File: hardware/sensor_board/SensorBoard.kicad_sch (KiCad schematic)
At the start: 28 parts, among them J1 EXT, J10 LED L2, J11 LED L3, J12 LED R1, J13 LED R2, J14 SPARE GPIO, J15 VSYS BUS, J16 GND BUS, J17 3V3 BUS, J2 SOIL SENSOR L, J3 SOIL SENSOR R, J4 ENV SENSOR L, J5 ENV SENSOR R, J6 FEED SENSOR L, J7 FEED SENSOR R, J8 LED R3, J9 LED L1, U1 Pico, U2 74HC595

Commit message: Brand new sensor board, includes I2C expander, RTC and relay board connections
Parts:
- added BT1: CR1220, Battery:BatteryHolder_Keystone_3000_1x12mm, symbol Device:Battery_Cell
- added C2: 0.1uf, Capacitor_THT:C_Disc_D6.0mm_W2.5mm_P5.00mm, symbol Device:C
- added D1, D2: 1N5820, Diode_THT:D_DO-201AD_P15.24mm_Horizontal, symbol Diode:1N5820
- added J1: Relay Board, Connector_PinHeader_2.54mm:PinHeader_1x10_P2.54mm_Vertical, symbol Connector_Generic:Conn_01x10
- added J15: LED L1, Connector_JST:JST_XH_B2B-XH-A_1x02_P2.50mm_Vertical, symbol Connector_Generic:Conn_02x01
- added J16: LED L2, Connector_JST:JST_XH_B2B-XH-A_1x02_P2.50mm_Vertical, symbol Connector_Generic:Conn_02x01
- added J2: Pi, Connector_JST:JST_XH_B2B-XH-A_1x02_P2.50mm_Vertical, symbol Connector:Screw_Terminal_01x02
- added J24: Raspberry Pi GPIO header, Connector_PinHeader_2.54mm:PinHeader_2x20_P2.54mm_Vertical, symbol Connector:Raspberry_Pi_2_3
- added J25: RTC Header, Connector_PinHeader_2.54mm:PinHeader_1x05_P2.54mm_Vertical, symbol Connector_Generic:Conn_01x05
- added J26: I2C3, Connector_JST:JST_XH_B4B-XH-A_1x04_P2.50mm_Vertical, symbol Connector_Generic:Conn_01x04
- added J27: I2C2, Connector_JST:JST_XH_B4B-XH-A_1x04_P2.50mm_Vertical, symbol Connector_Generic:Conn_01x04
- added J28: I2C1, Connector_JST:JST_XH_B4B-XH-A_1x04_P2.50mm_Vertical, symbol Connector_Generic:Conn_01x04
- added J29: I2C4, Connector_JST:JST_XH_B4B-XH-A_1x04_P2.50mm_Vertical, symbol Connector_Generic:Conn_01x04
- added J3: Display, Connector_JST:JST_XH_B2B-XH-A_1x02_P2.50mm_Vertical, symbol Connector:Screw_Terminal_01x02
- added J30: I2C5, Connector_JST:JST_XH_B4B-XH-A_1x04_P2.50mm_Vertical, symbol Connector_Generic:Conn_01x04
- added J31: I2C6, Connector_JST:JST_XH_B4B-XH-A_1x04_P2.50mm_Vertical, symbol Connector_Generic:Conn_01x04
- added J32: I2C7, Connector_JST:JST_XH_B4B-XH-A_1x04_P2.50mm_Vertical, symbol Connector_Generic:Conn_01x04
- added J4: DC IN 5V, Connector_BarrelJack:BarrelJack_Horizontal, symbol Connector:Barrel_Jack
- added Q1, Q2, Q3, Q4, Q5, Q6, Q7, Q8: PN2222A, Package_TO_SOT_THT:TO-92_Inline, symbol Transistor_BJT:PN2222A
- added R1, R2, R3, R4, R5, R6, R7, R8: 2.2k, Resistor_THT:R_Axial_DIN0207_L6.3mm_D2.5mm_P7.62mm_Horizontal, symbol Device:R
- added R11, R12: R1, Resistor_THT:R_Axial_DIN0207_L6.3mm_D2.5mm_P7.62mm_Horizontal, symbol Device:R
- added R19, R20: 4.3k, Resistor_THT:R_Axial_DIN0207_L6.3mm_D2.5mm_P7.62mm_Horizontal, symbol Device:R
- added RN1, RN2: 10k, Resistor_THT:R_Array_SIP9, symbol Device:R_Network08
- added SW1: Reset, Button_Switch_THT:SW_PUSH_6mm, symbol Switch:SW_Push
- added U3: TCA9548A, Package_DIP:DIP-24_W15.24mm, symbol Interface_Expansion:TCA9548A_Adafruit
- added U4: LM1117, Package_TO_SOT_THT:TO-220-3_Horizontal_TabDown, symbol Regulator_Linear:LM1117-3.3
- added U5: DS3231MZ, Package_SO:SOIC-8_3.9x4.9mm_P1.27mm, symbol Timer_RTC:DS3231MZ
- J12: renamed from J4; value ENV SENSOR L -> DHT22 R
- J14: renamed from J5; value ENV SENSOR R -> DHT22 L
- J17: renamed from J8; value LED R3 -> LED L3
- J18: renamed from J9; value LED L1 -> LED L4
- J19: renamed from J10; value LED L2 -> LED R1
- J21: renamed from J11; value LED L3 -> LED R2
- J22: renamed from J12; value LED R1 -> LED R3
- J23: renamed from J13; value LED R2 -> LED R4
- U1: value Pico -> Raspberry Pico
- renumbered J16 to J10, J7 to J11, J14 to J13, J1 to J20, J15 to J5, J2 to J6, J17 to J7, J6 to J8, J3 to J9, R8 to R10, R1 to R13, R2 to R14, R3 to R15, R4 to R16, R5 to R17, R6 to R18, R7 to R9
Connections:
- net +3V3: now also J26.1 (Pin_1), J27.1 (Pin_1), J28.1 (Pin_1), J29.1 (Pin_1), J30.1 (Pin_1), J31.1 (Pin_1), J32.1 (Pin_1), U3.1 (VCC), U4.2 (VO); no longer U1.36 (3V3)
- net CTL RX: now also J24.8 (GPIO14/TXD)
- net CTL TX: now also J24.10 (GPIO15/RXD)
- net ENV SENSOR L CTL: now also J14.2 (Pin_2), R10.1, U1.20 (GPIO15); no longer J12.2 (Pin_2), R9.1, U1.19 (GPIO14)
- net ENV SENSOR R CTL: now also J12.2 (Pin_2), R9.1, U1.19 (GPIO14); no longer J14.2 (Pin_2), R10.1, U1.20 (GPIO15)
- net GND: now also BT1.2 (-), C2.2, J1.1 (Pin_1), J15.1 (Pin_1), J16.1 (Pin_1), J2.2 (Pin_2), J24.14 (GND), J24.20 (GND), J24.25 (GND), J24.30 (GND), J24.34 (GND), J24.39 (GND), J24.6 (GND), J24.9 (GND), J25.1 (Pin_1), J26.4 (Pin_4), J27.4 (Pin_4), J28.4 (Pin_4), J29.4 (Pin_4), J3.2 (Pin_2), J30.4 (Pin_4), J31.4 (Pin_4), J32.4 (Pin_4), J4.2, Q1.1 (E), Q2.1 (E), Q3.1 (E), Q4.1 (E), Q5.1 (E), Q6.1 (E), Q7.1 (E), Q8.1 (E), RN1.1 (common), SW1.1, U3.2 (GND), U4.1 (GND), U5.5 (GND)
- net I2C1 SCL: now also U3.4 (SCL); no longer J6.5 (Pin_5), J9.5 (Pin_5)
- net I2C1 SDA: now also U3.3 (SDA); no longer J6.2 (Pin_2), J9.2 (Pin_2)
- net VS: now also D1.1 (K), D2.1 (K), J1.10 (Pin_10), J2.1 (Pin_1), J3.1 (Pin_1), RN2.1 (common), U4.3 (VI); no longer J20.1 (Pin_1)
- net at U2.1 (QB): now also R12.1
- net at U2.15 (QA): now also R11.1
- net at U1.30 (RUN): now also SW1.2
- net ENV SENSOR L DETECT renamed DHT22 L DETECT
- net DHT22 L DETECT: now also J14.4 (Pin_4); no longer J12.4 (Pin_4)
- net ENV SENSOR R DETECT renamed DHT22 R DETECT
- net DHT22 R DETECT: now also J12.4 (Pin_4); no longer J14.4 (Pin_4)
- new net: Q6.2 (B), R6.2
- new net: J1.7 (Pin_7), Q6.3 (C), RN2.4 (R3)
- new net: J15.2 (Pin_2), R11.2
- new net: Q1.2 (B), R1.2
- new net: J1.2 (Pin_2), Q1.3 (C), RN2.9 (R8)
- new net: J32.2 (Pin_2), U3.23 (SD7)
- new net: J32.3 (Pin_3), U3.24 (SC7)
- new net: J16.2 (Pin_2), R12.2
- new net: J1.9 (Pin_9), Q8.3 (C), RN2.2 (R1)
- new net: J1.8 (Pin_8), Q7.3 (C), RN2.3 (R2)
- new net: J1.6 (Pin_6), Q5.3 (C), RN2.5 (R4)
- new net: J1.5 (Pin_5), Q4.3 (C), RN2.6 (R5)
- new net: J1.4 (Pin_4), Q3.3 (C), RN2.7 (R6)
- new net: J1.3 (Pin_3), Q2.3 (C), RN2.8 (R7)
- new net: J24.40 (GPIO21/SCLK1), R8.1, RN1.9 (R8)
- new net: Q8.2 (B), R8.2
- new net: BT1.1 (+), U5.6 (VBAT)
- new net: J24.32 (PWM0/GPIO12), R2.1, RN1.3 (R2)
- new net: Q2.2 (B), R2.2
- new net: J6.2 (Pin_2), J9.2 (Pin_2), U3.9 (SD0)
- new net: J6.5 (Pin_5), J9.5 (Pin_5), U3.10 (SC0)
- new net: J29.2 (Pin_2), U3.17 (SD4)
- new net: J29.3 (Pin_3), U3.18 (SC4)
- new net: J28.2 (Pin_2), U3.11 (SD1)
- new net: J28.3 (Pin_3), U3.12 (SC1)
- new net: J26.2 (Pin_2), U3.15 (SD3)
- new net: J26.3 (Pin_3), U3.16 (SC3)
- new net: C2.1, J24.1 (3V3), J25.5 (Pin_5), R19.1, R20.1, U5.2 (VCC)
- new net: J24.5 (SCL/GPIO3), J25.3 (Pin_3), R20.2, U5.8 (SCL)
- new net: J27.2 (Pin_2), U3.13 (SD2)
- new net: J27.3 (Pin_3), U3.14 (SC2)
- new net: J30.2 (Pin_2), U3.19 (SD5)
- new net: J30.3 (Pin_3), U3.20 (SC5)
- new net: J31.2 (Pin_2), U3.21 (SD6)
- new net: J31.3 (Pin_3), U3.22 (SC6)
- new net: J24.29 (GCLK1/GPIO5), R1.1, RN1.2 (R1)
- new net: J24.3 (SDA/GPIO2), J25.4 (Pin_4), R19.2, U5.7 (SDA)
- new net: J24.31 (GCLK2/GPIO6), R3.1, RN1.4 (R3)
- new net: J24.33 (PWM1/GPIO13), R4.1, RN1.5 (R4)
- new net: J24.35 (GPIO19/MISO1), R6.1, RN1.7 (R6)
- new net: J24.36 (GPIO16), R5.1, RN1.6 (R5)
- new net: J24.38 (GPIO20/MOSI1), R7.1, RN1.8 (R7)
- new net: Q3.2 (B), R3.2
- new net: Q7.2 (B), R7.2
- new net: D2.2 (A), J4.1
- new net: Q4.2 (B), R4.2
- new net: Q5.2 (B), R5.2
- new net VSYS: D1.2 (A), J20.1 (Pin_1)
- no-connect marks 8 -> 33
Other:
- moved on the sheet: C1, J10, J11, J12, J13, J14, J17, J18, J19, J20, J21, J22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

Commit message: New version without DHT22. Full exposed I2C expander
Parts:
- removed J12: DHT22 R, Connector_JST:JST_XH_B4B-XH-A_1x04_P2.50mm_Vertical, symbol Connector_Generic:Conn_01x04
- removed J14: DHT22 L, Connector_JST:JST_XH_B4B-XH-A_1x04_P2.50mm_Vertical, symbol Connector_Generic:Conn_01x04
- removed R10: R8, Resistor_THT:R_Axial_DIN0207_L6.3mm_D2.5mm_P7.62mm_Horizontal, symbol Device:R
- removed R9: R7, Resistor_THT:R_Axial_DIN0207_L6.3mm_D2.5mm_P7.62mm_Horizontal, symbol Device:R
- added C3: 0.1uf, Capacitor_THT:C_Disc_D6.0mm_W2.5mm_P5.00mm, symbol Device:C
- added J26: I2C0, Connector_JST:JST_XH_B5B-XH-A_1x05_P2.50mm_Vertical, symbol Connector_Generic:Conn_01x05
- added RN3: 10k, Resistor_THT:R_Array_SIP9, symbol Device:R_Network08
- added U6: 74HC165, Package_DIP:DIP-16_W7.62mm, symbol 74xx:74HC165
- J13: footprint Connector_PinHeader_2.54mm:PinHeader_1x05_P2.54mm_Vertical -> Connector_PinHeader_2.54mm:PinHeader_1x04_P2.54mm_Vertical; symbol Connector_Generic:Conn_01x05 -> Connector_Generic:Conn_01x04
- J27: renamed from J28; footprint Connector_JST:JST_XH_B4B-XH-A_1x04_P2.50mm_Vertical -> Connector_JST:JST_XH_B5B-XH-A_1x05_P2.50mm_Vertical; symbol Connector_Generic:Conn_01x04 -> Connector_Generic:Conn_01x05
- J28: renamed from J27; footprint Connector_JST:JST_XH_B4B-XH-A_1x04_P2.50mm_Vertical -> Connector_JST:JST_XH_B5B-XH-A_1x05_P2.50mm_Vertical; symbol Connector_Generic:Conn_01x04 -> Connector_Generic:Conn_01x05
- J29: renamed from J26; footprint Connector_JST:JST_XH_B4B-XH-A_1x04_P2.50mm_Vertical -> Connector_JST:JST_XH_B5B-XH-A_1x05_P2.50mm_Vertical; symbol Connector_Generic:Conn_01x04 -> Connector_Generic:Conn_01x05
- J30: renamed from J29; footprint Connector_JST:JST_XH_B4B-XH-A_1x04_P2.50mm_Vertical -> Connector_JST:JST_XH_B5B-XH-A_1x05_P2.50mm_Vertical; symbol Connector_Generic:Conn_01x04 -> Connector_Generic:Conn_01x05
- J31: renamed from J30; footprint Connector_JST:JST_XH_B4B-XH-A_1x04_P2.50mm_Vertical -> Connector_JST:JST_XH_B5B-XH-A_1x05_P2.50mm_Vertical; symbol Connector_Generic:Conn_01x04 -> Connector_Generic:Conn_01x05
- J32: renamed from J31; footprint Connector_JST:JST_XH_B4B-XH-A_1x04_P2.50mm_Vertical -> Connector_JST:JST_XH_B5B-XH-A_1x05_P2.50mm_Vertical; symbol Connector_Generic:Conn_01x04 -> Connector_Generic:Conn_01x05
- J33: renamed from J32; footprint Connector_JST:JST_XH_B4B-XH-A_1x04_P2.50mm_Vertical -> Connector_JST:JST_XH_B5B-XH-A_1x05_P2.50mm_Vertical; symbol Connector_Generic:Conn_01x04 -> Connector_Generic:Conn_01x05
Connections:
- net DHT22 L DETECT is gone; now on an unnamed net: U1.6 (GPIO4)
- net DHT22 R DETECT is gone; now on an unnamed net: U1.7 (GPIO5)
- net +3V3: now also C3.1, J26.1 (Pin_1), RN3.1 (common), U6.16 (VCC)
- net GND: now also J27.5 (Pin_5), J28.5 (Pin_5), J29.5 (Pin_5), J30.5 (Pin_5), J31.5 (Pin_5), J32.5 (Pin_5), J33.5 (Pin_5), C3.2, J26.5 (Pin_5), U6.10 (DS), U6.15 (~{CE}), U6.8 (GND); no longer J27.4 (Pin_4), J28.4 (Pin_4), J29.4 (Pin_4), J30.4 (Pin_4), J31.4 (Pin_4), J32.4 (Pin_4), J33.4 (Pin_4)
- net at J6.2 (Pin_2), J9.2 (Pin_2): no longer U3.9 (SD0)
- net at J6.5 (Pin_5), J9.5 (Pin_5): no longer U3.10 (SC0)
- net ENV SENSOR L CTL renamed GPIO15
- net GPIO15: now also J13.4 (Pin_4)
- net ENV SENSOR R CTL: no longer names the net of U1.19 (GPIO14)
- net ENV SENSOR R CTL: now also U6.1 (~{PL})
- net GPIO10: no longer names the net of U1.14 (GPIO10)
- net GPIO10: now also U6.9 (Q7); no longer J13.5 (Pin_5)
- net GPIO11: no longer names the net of U1.15 (GPIO11)
- net GPIO11: now also U6.2 (CP); no longer J13.4 (Pin_4)
- new net: J33.4 (Pin_4), RN3.2 (R1), U6.6 (D7)
- new net: J26.4 (Pin_4), RN3.9 (R8), U6.11 (D0)
- new net: J27.4 (Pin_4), RN3.8 (R7), U6.12 (D1)
- new net: J28.4 (Pin_4), RN3.7 (R6), U6.13 (D2)
- new net: J29.4 (Pin_4), RN3.6 (R5), U6.14 (D3)
- new net: J30.4 (Pin_4), RN3.5 (R4), U6.3 (D4)
- new net: J31.4 (Pin_4), RN3.4 (R3), U6.4 (D5)
- new net: J32.4 (Pin_4), RN3.3 (R2), U6.5 (D6)
- new net: J26.3 (Pin_3), U3.10 (SC0)
- new net: J26.2 (Pin_2), U3.9 (SD0)
- no-connect marks 33 -> 34
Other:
- moved on the sheet: BT1, C1, C2, D1, D2, J1, J10, J11, J15, J16, J17, J18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

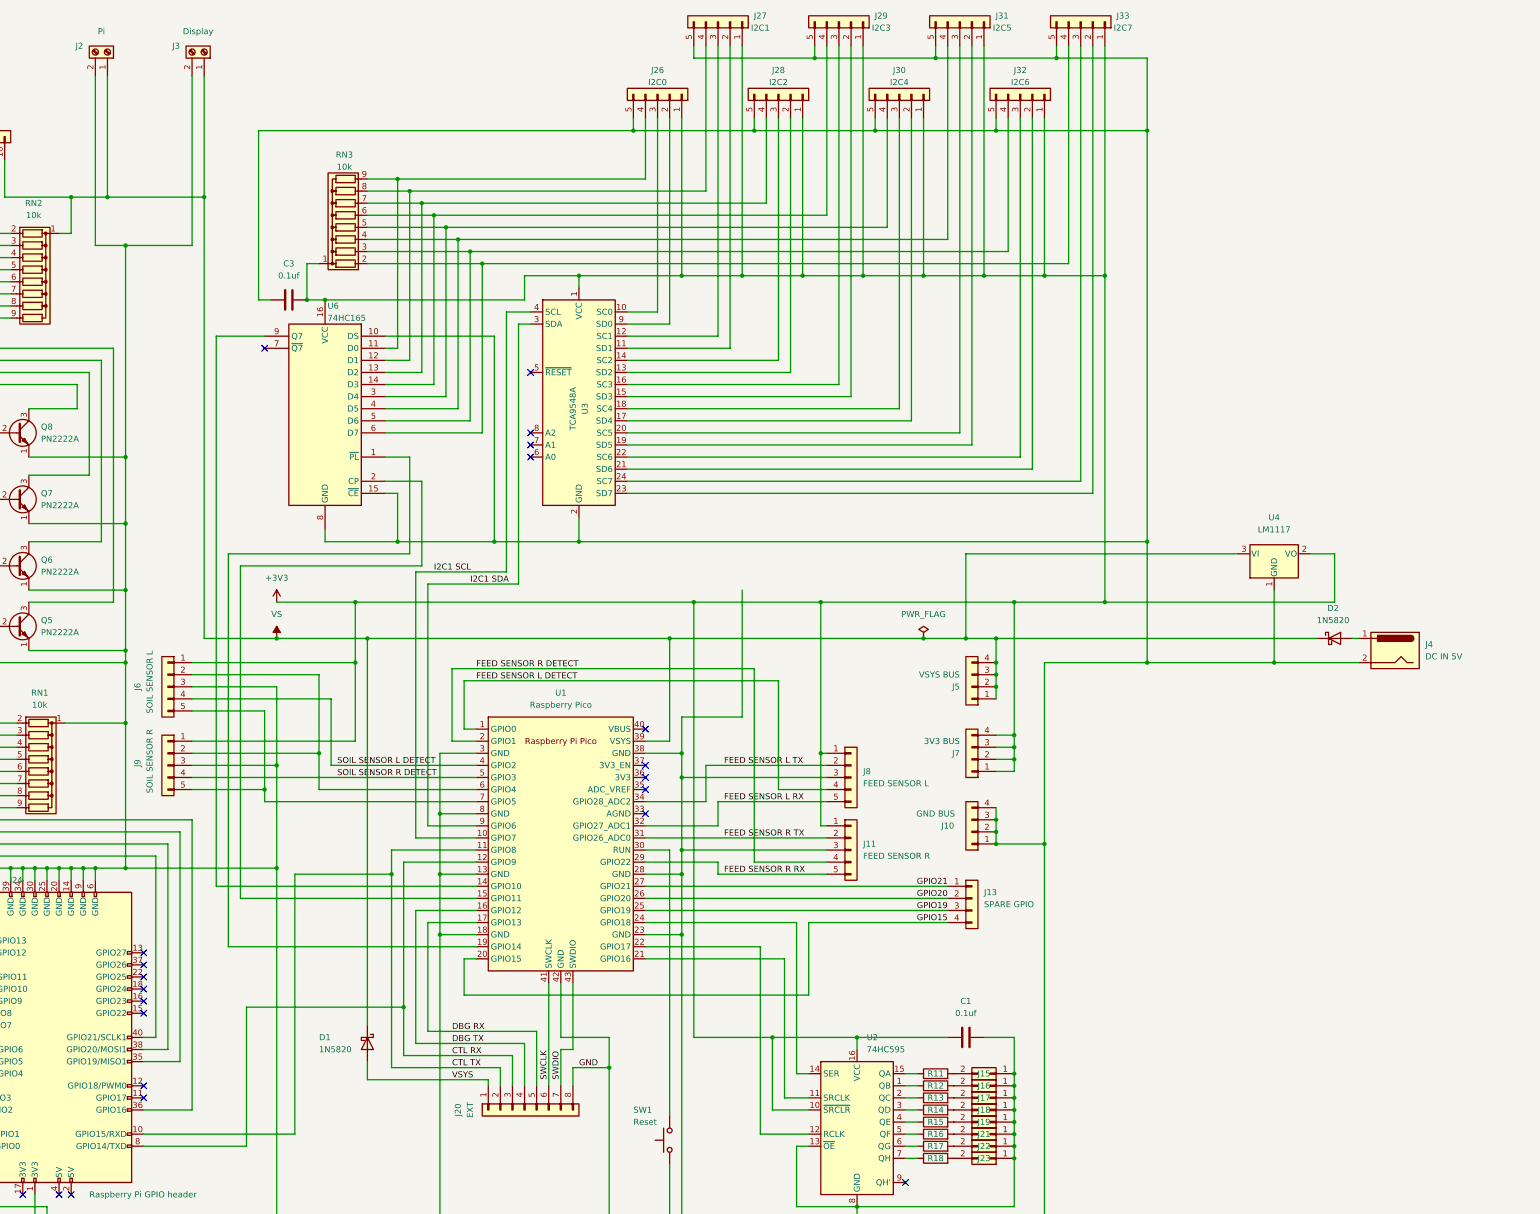
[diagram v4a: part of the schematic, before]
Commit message: Completely revamped board. Will fully use the I2C expander now to have one "sensor pod" per grow system containing an SCD30 and a soil sensor. This allows for 8 sensor pods. Will reuse the I2C interface for the soil sensors for additional feed level sonar sensors.
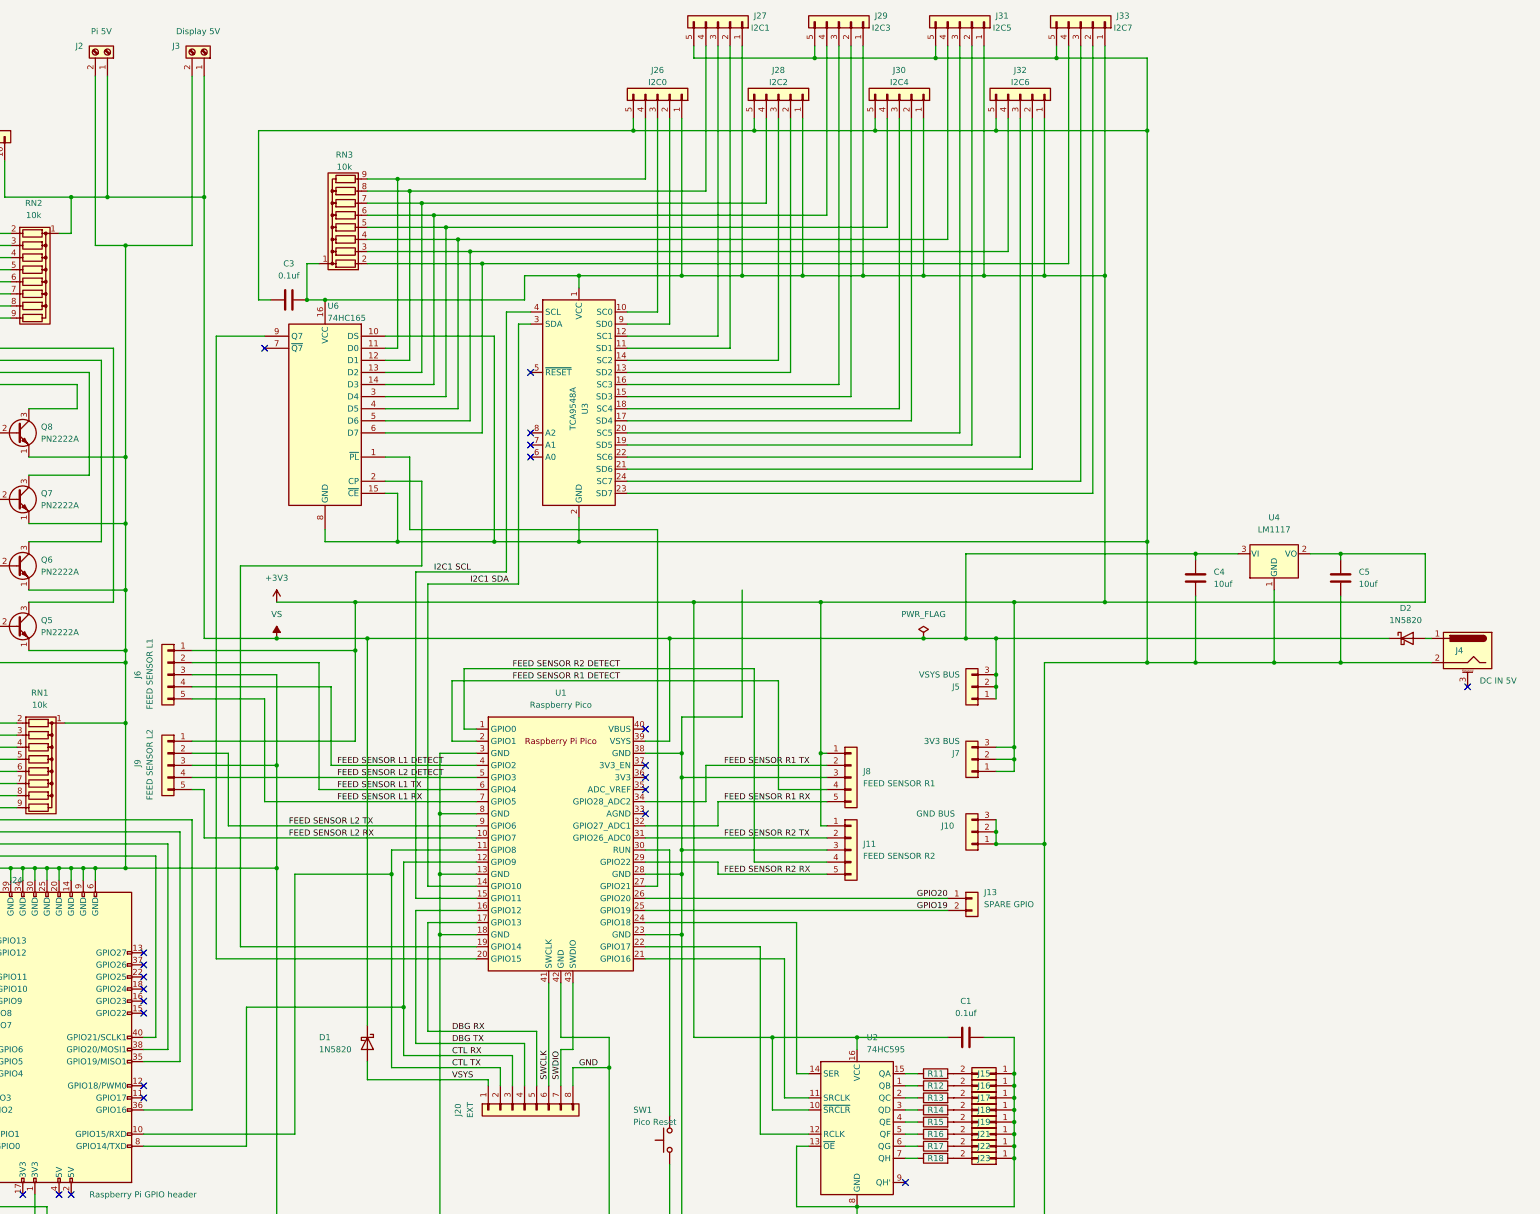
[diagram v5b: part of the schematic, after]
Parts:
- added C4, C5: 10uf, Capacitor_THT:C_Disc_D6.0mm_W2.5mm_P5.00mm, symbol Device:C
- J10, J5, J7: footprint Connector_PinHeader_2.54mm:PinHeader_1x04_P2.54mm_Vertical -> Connector_PinHeader_2.54mm:PinHeader_1x03_P2.54mm_Vertical; symbol Connector_Generic:Conn_01x04 -> Connector_Generic:Conn_01x03
- J11: value FEED SENSOR R -> FEED SENSOR R2
- J13: footprint Connector_PinHeader_2.54mm:PinHeader_1x04_P2.54mm_Vertical -> Connector_PinHeader_2.54mm:PinHeader_1x02_P2.54mm_Vertical; symbol Connector_Generic:Conn_01x04 -> Connector_Generic:Conn_01x02
- J2: value Pi -> Pi 5V
- J3: value Display -> Display 5V
- J4: symbol Connector:Barrel_Jack -> Connector:Barrel_Jack_MountingPin
- J6: value SOIL SENSOR L -> FEED SENSOR L1
- J8: value FEED SENSOR L -> FEED SENSOR R1
- J9: value SOIL SENSOR R -> FEED SENSOR L2
- SW1: value Reset -> Pico Reset
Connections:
- net +3V3: now also C5.1; no longer J7.4 (Pin_4)
- net GND: now also C4.1, C5.2; no longer J10.4 (Pin_4)
- net GPIO19: now also J13.2 (Pin_2); no longer J13.3 (Pin_3)
- net GPIO20: now also J13.1 (Pin_1); no longer J13.2 (Pin_2)
- net I2C1 SCL: now also U1.15 (GPIO11); no longer U1.10 (GPIO7)
- net I2C1 SDA: now also U1.14 (GPIO10); no longer U1.9 (GPIO6)
- net VS: now also C4.2; no longer J5.4 (Pin_4)
- net at U6.1 (~{PL}): now also U1.27 (GPIO21); no longer U1.19 (GPIO14)
- net at U6.2 (CP): now also U1.19 (GPIO14); no longer U1.15 (GPIO11)
- net at U6.9 (Q7): now also U1.20 (GPIO15); no longer U1.14 (GPIO10)
- net FEED SENSOR L1 TX: now reaches J6.2 (Pin_2), U1.6 (GPIO4)
- net FEED SENSOR L1 TX: no longer J9.2 (Pin_2)
- net FEED SENSOR L1 RX: now reaches J6.5 (Pin_5), U1.7 (GPIO5)
- net FEED SENSOR L1 RX: no longer J9.5 (Pin_5)
- net FEED SENSOR L DETECT renamed FEED SENSOR R1 DETECT
- net FEED SENSOR R1 DETECT: now also U1.2 (GPIO1); no longer U1.1 (GPIO0)
- net FEED SENSOR L RX renamed FEED SENSOR R1 RX
- net FEED SENSOR L TX renamed FEED SENSOR R1 TX
- net FEED SENSOR R DETECT renamed FEED SENSOR R2 DETECT
- net FEED SENSOR R2 DETECT: now also U1.1 (GPIO0); no longer U1.2 (GPIO1)
- net FEED SENSOR R RX renamed FEED SENSOR R2 RX
- net FEED SENSOR R TX renamed FEED SENSOR R2 TX
- removed net GPIO15: J13.4 (Pin_4), U1.20 (GPIO15)
- removed net GPIO21: J13.1 (Pin_1), U1.27 (GPIO21)
- net SOIL SENSOR L DETECT renamed FEED SENSOR L1 DETECT
- net SOIL SENSOR R DETECT renamed FEED SENSOR L2 DETECT
- new net FEED SENSOR L2 RX: J9.5 (Pin_5), U1.10 (GPIO7)
- new net FEED SENSOR L2 TX: J9.2 (Pin_2), U1.9 (GPIO6)
- no-connect marks 34 -> 35
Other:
- moved on the sheet: D2, J6

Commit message: Beautifying board
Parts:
- J1: value Relay Board -> Relay Board Connector
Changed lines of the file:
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@@
     (in_bom yes) (on_board yes) (fields_autoplaced)
     (property "Reference" "J1" (id 0) (at 57.15 34.29 90))
-    (property "Value" "Relay Board" (id 1) (at 57.15 36.83 90))
+    (property "Value" "Relay Board Connector" (id 1) (at 57.15 36.83 90))
     (property "Footprint" "Connector_PinHeader_2.54mm:PinHeader_1x10_P2.54mm_Vertical" (id 2) (at 55.88 40.64 0)
       (effects (font (size 1.27 1.27)) hide)
@@
     )
     (path "/400f4f70-20bc-4cf8-874a-a91123f3236d"
-      (reference "J1") (unit 1) (value "Relay Board") (footprint "Connector_PinHeader_2.54mm:PinHeader_1x10_P2.54mm_Vertical")
+      (reference "J1") (unit 1) (value "Relay Board Connector") (footprint "Connector_PinHeader_2.54mm:PinHeader_1x10_P2.54mm_Vertical")
     )
     (path "/4bc375fb-4352-4621-9522-ce2db829d67f"
